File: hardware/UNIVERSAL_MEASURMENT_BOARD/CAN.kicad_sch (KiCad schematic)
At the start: 17 parts, among them U16 ADM3057EBRWZ

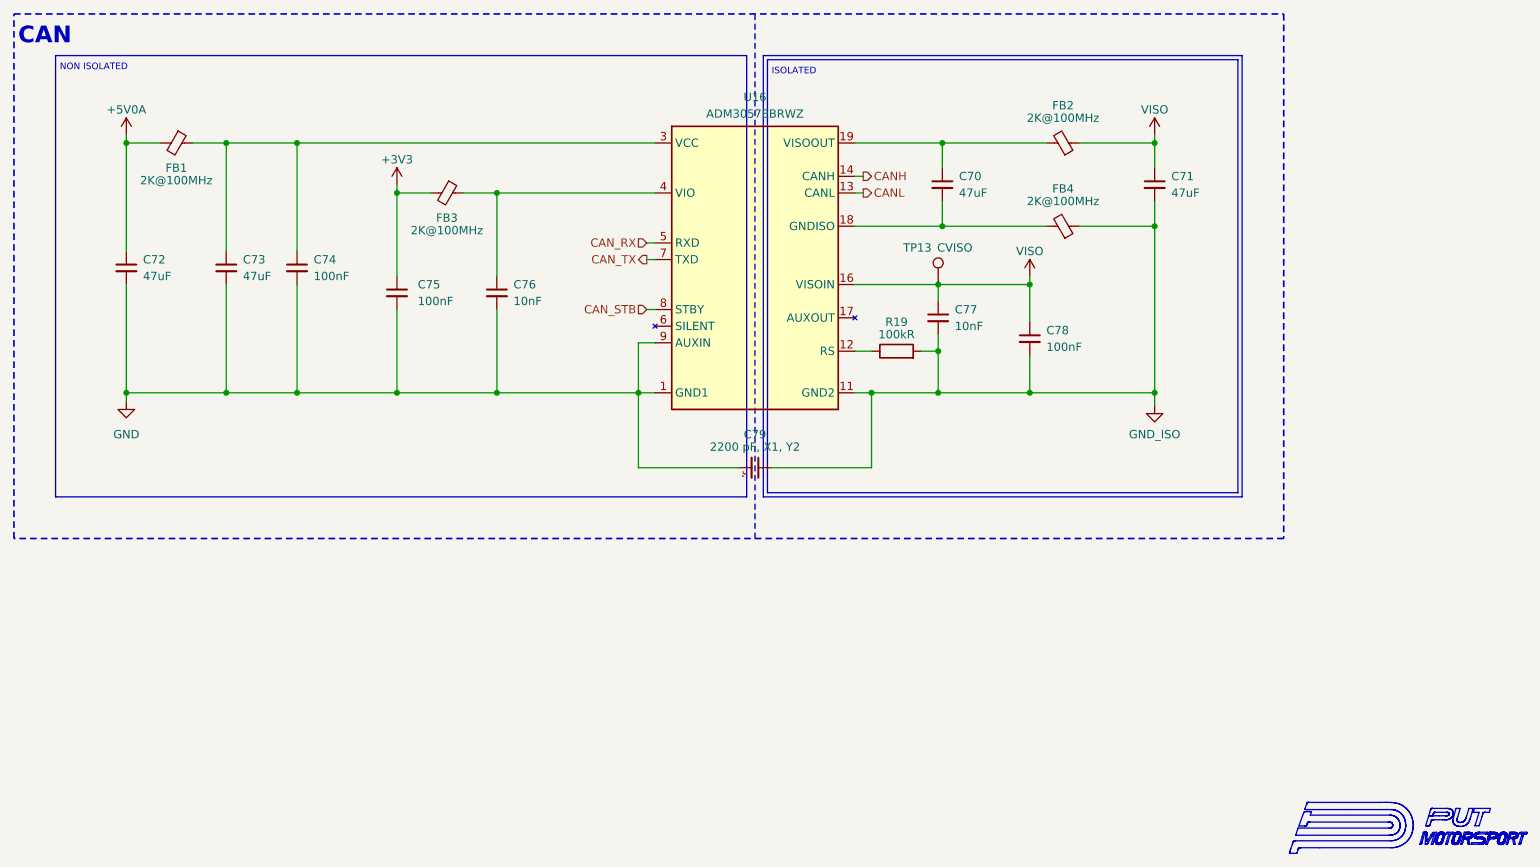
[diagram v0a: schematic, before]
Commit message: Update power section:
- Change input capacitor configuration to 1 per inductor in ±18V converter

- Add ±18V DC/DC, 12V LDO, and 5V LDO layouts

- Add TVS diodes and fuses to the measurement path
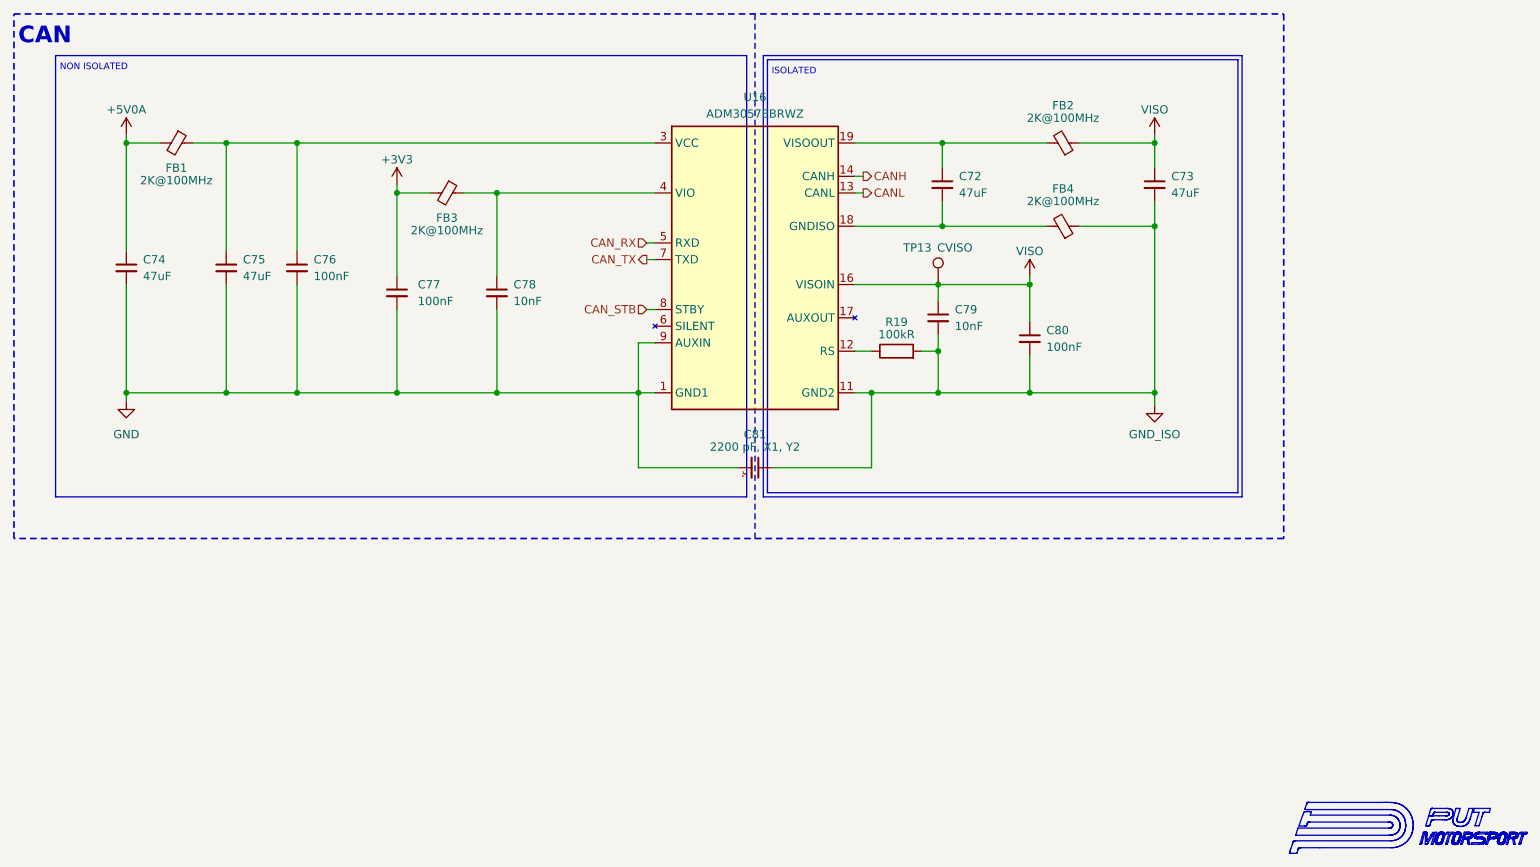
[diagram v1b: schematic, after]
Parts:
- renumbered C70 to C72, C71 to C73, C72 to C74, C73 to C75, C74 to C76, C75 to C77, C76 to C78, C77 to C79, C78 to C80, C79 to C81
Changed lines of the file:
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@@
 		(dnp no)
 		(fields_autoplaced yes)
-		(property "Reference" "C74"
+		(property "Reference" "C76"
 			(at 97.155 87.0012 0)
 			(show_name no)
@@
 			(project "UNIVERSAL_MEASURMENT_BOARD"
 				(path "/92c00310-4384-4ef3-9368-efad75526047/007c1dd5-a7d9-42e3-b7c2-f5a2b9d94f0b"
-					(reference "C74")
+					(reference "C76")
 					(unit 1)
 				)
@@
 		(in_pos_files yes)
 		(dnp no)
-		(property "Reference" "C79"
+		(property "Reference" "C81"
 			(at 164.465 113.665 0)
 			(show_name no)
@@
 			(project "UNIVERSAL_MEASURMENT_BOARD"
 				(path "/92c00310-4384-4ef3-9368-efad75526047/007c1dd5-a7d9-42e3-b7c2-f5a2b9d94f0b"
-					(reference "C79")
+					(reference "C81")
 					(unit 1)
 				)
@@
 		(in_pos_files yes)
 		(dnp no)
-		(property "Reference" "C70"
+		(property "Reference" "C72"
 			(at 195.58 74.295 0)
 			(show_name no)
@@
 			(project "UNIVERSAL_MEASURMENT_BOARD"
 				(path "/92c00310-4384-4ef3-9368-efad75526047/007c1dd5-a7d9-42e3-b7c2-f5a2b9d94f0b"
-					(reference "C70")
+					(reference "C72")
 					(unit 1)
 				)
@@
 		(in_pos_files yes)
 		(dnp no)
-		(property "Reference" "C71"
+		(property "Reference" "C73"
 			(at 227.965 74.3012 0)
 			(show_name no)
@@
 			(project "UNIVERSAL_MEASURMENT_BOARD"
 				(path "/92c00310-4384-4ef3-9368-efad75526047/007c1dd5-a7d9-42e3-b7c2-f5a2b9d94f0b"
-					(reference "C71")
+					(reference "C73")
 					(unit 1)
 				)
@@
 		(dnp no)
 		(fields_autoplaced yes)
-		(property "Reference" "C77"
+		(property "Reference" "C79"
 			(at 194.945 94.6212 0)
 			(show_name no)
@@
 			(project "UNIVERSAL_MEASURMENT_BOARD"
 				(path "/92c00310-4384-4ef3-9368-efad75526047/007c1dd5-a7d9-42e3-b7c2-f5a2b9d94f0b"
-					(reference "C77")
+					(reference "C79")
 					(unit 1)
 				)
@@
 		(dnp no)
 		(fields_autoplaced yes)
-		(property "Reference" "#PWR0159"
+		(property "Reference" "#PWR0161"
 			(at 225.425 115.57 0)
 			(hide yes)
@@
 			(project "UNIVERSAL_MEASURMENT_BOARD"
 				(path "/92c00310-4384-4ef3-9368-efad75526047/007c1dd5-a7d9-42e3-b7c2-f5a2b9d94f0b"
-					(reference "#PWR0159")
+					(reference "#PWR0161")
 					(unit 1)
 				)
@@
 		(dnp no)
 		(fields_autoplaced yes)
-		(property "Reference" "#PWR0158"
+		(property "Reference" "#PWR0160"
 			(at 68.58 114.935 0)
 			(hide yes)
@@
 			(project "UNIVERSAL_MEASURMENT_BOARD"
 				(path "/92c00310-4384-4ef3-9368-efad75526047/007c1dd5-a7d9-42e3-b7c2-f5a2b9d94f0b"
-					(reference "#PWR0158")
+					(reference "#PWR0160")
 					(unit 1)
 				)
@@
 		(in_pos_files yes)
 		(dnp no)
-		(property "Reference" "#PWR0155"
+		(property "Reference" "#PWR0157"
 			(at 225.425 71.755 0)
 			(hide yes)
@@
 			(project "UNIVERSAL_MEASURMENT_BOARD"
 				(path "/92c00310-4384-4ef3-9368-efad75526047/007c1dd5-a7d9-42e3-b7c2-f5a2b9d94f0b"
-					(reference "#PWR0155")
+					(reference "#PWR0157")
 					(unit 1)
 				)
@@
 		(dnp no)
 		(fields_autoplaced yes)
-		(property "Reference" "C76"
+		(property "Reference" "C78"
 			(at 127.635 90.8112 0)
 			(show_name no)
@@
 			(project "UNIVERSAL_MEASURMENT_BOARD"
 				(path "/92c00310-4384-4ef3-9368-efad75526047/007c1dd5-a7d9-42e3-b7c2-f5a2b9d94f0b"
-					(reference "C76")
+					(reference "C78")
 					(unit 1)
 				)
@@
 		(dnp no)
 		(fields_autoplaced yes)
-		(property "Reference" "C78"
+		(property "Reference" "C80"
 			(at 208.915 97.7962 0)
 			(show_name no)
@@
 			(project "UNIVERSAL_MEASURMENT_BOARD"
 				(path "/92c00310-4384-4ef3-9368-efad75526047/007c1dd5-a7d9-42e3-b7c2-f5a2b9d94f0b"
-					(reference "C78")
+					(reference "C80")
 					(unit 1)
 				)
@@
 		(in_pos_files yes)
 		(dnp no)
-		(property "Reference" "#PWR0157"
+		(property "Reference" "#PWR0159"
 			(at 206.375 93.345 0)
 			(hide yes)
@@
 			(project "UNIVERSAL_MEASURMENT_BOARD"
 				(path "/92c00310-4384-4ef3-9368-efad75526047/007c1dd5-a7d9-42e3-b7c2-f5a2b9d94f0b"
-					(reference "#PWR0157")
+					(reference "#PWR0159")
 					(unit 1)
 				)
@@
 		(dnp no)
 		(fields_autoplaced yes)
-		(property "Reference" "C72"
+		(property "Reference" "C74"
 			(at 71.12 87.0012 0)
 			(show_name no)
@@
 			(project "UNIVERSAL_MEASURMENT_BOARD"
 				(path "/92c00310-4384-4ef3-9368-efad75526047/007c1dd5-a7d9-42e3-b7c2-f5a2b9d94f0b"
-					(reference "C72")
+					(reference "C74")
 					(unit 1)
 				)
@@
 		(dnp no)
 		(fields_autoplaced yes)
-		(property "Reference" "C75"
+		(property "Reference" "C77"
 			(at 113.03 90.8112 0)
 			(show_name no)
@@
 			(project "UNIVERSAL_MEASURMENT_BOARD"
 				(path "/92c00310-4384-4ef3-9368-efad75526047/007c1dd5-a7d9-42e3-b7c2-f5a2b9d94f0b"
-					(reference "C75")
+					(reference "C77")
 					(unit 1)
 				)
@@
 		(in_pos_files yes)
 		(dnp no)
-		(property "Reference" "#PWR0156"
+		(property "Reference" "#PWR0158"
 			(at 109.855 79.375 0)
 			(hide yes)
@@
 			(project "UNIVERSAL_MEASURMENT_BOARD"
 				(path "/92c00310-4384-4ef3-9368-efad75526047/007c1dd5-a7d9-42e3-b7c2-f5a2b9d94f0b"
-					(reference "#PWR0156")
+					(reference "#PWR0158")
 					(unit 1)
 				)
@@
 		(in_pos_files yes)
 		(dnp no)
-		(property "Reference" "#PWR0154"
+		(property "Reference" "#PWR0156"
 			(at 68.58 71.755 0)
 			(hide yes)
@@
 			(project "UNIVERSAL_MEASURMENT_BOARD"
 				(path "/92c00310-4384-4ef3-9368-efad75526047/007c1dd5-a7d9-42e3-b7c2-f5a2b9d94f0b"
-					(reference "#PWR0154")
+					(reference "#PWR0156")
 					(unit 1)
 				)
@@
 		(dnp no)
 		(fields_autoplaced yes)
-		(property "Reference" "C73"
+		(property "Reference" "C75"
 			(at 86.36 87.0012 0)
 			(show_name no)
@@
 			(project "UNIVERSAL_MEASURMENT_BOARD"
 				(path "/92c00310-4384-4ef3-9368-efad75526047/007c1dd5-a7d9-42e3-b7c2-f5a2b9d94f0b"
-					(reference "C73")
-					(unit 1)
-				)
+					(reference "C75")
+					(unit 1)
+				)
